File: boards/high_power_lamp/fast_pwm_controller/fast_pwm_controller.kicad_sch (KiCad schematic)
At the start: 26 parts, among them J1 Screw_Terminal_01x02, J2 Screw_Terminal_01x02, J3 Screw_Terminal_01x02, J4 Screw_Terminal_01x02, J5 Screw_Terminal_01x02, J6 Screw_Terminal_01x02, J7 Screw_Terminal_01x02, J8 Screw_Terminal_01x02, J9 Screw_Terminal_01x02, U1 4050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

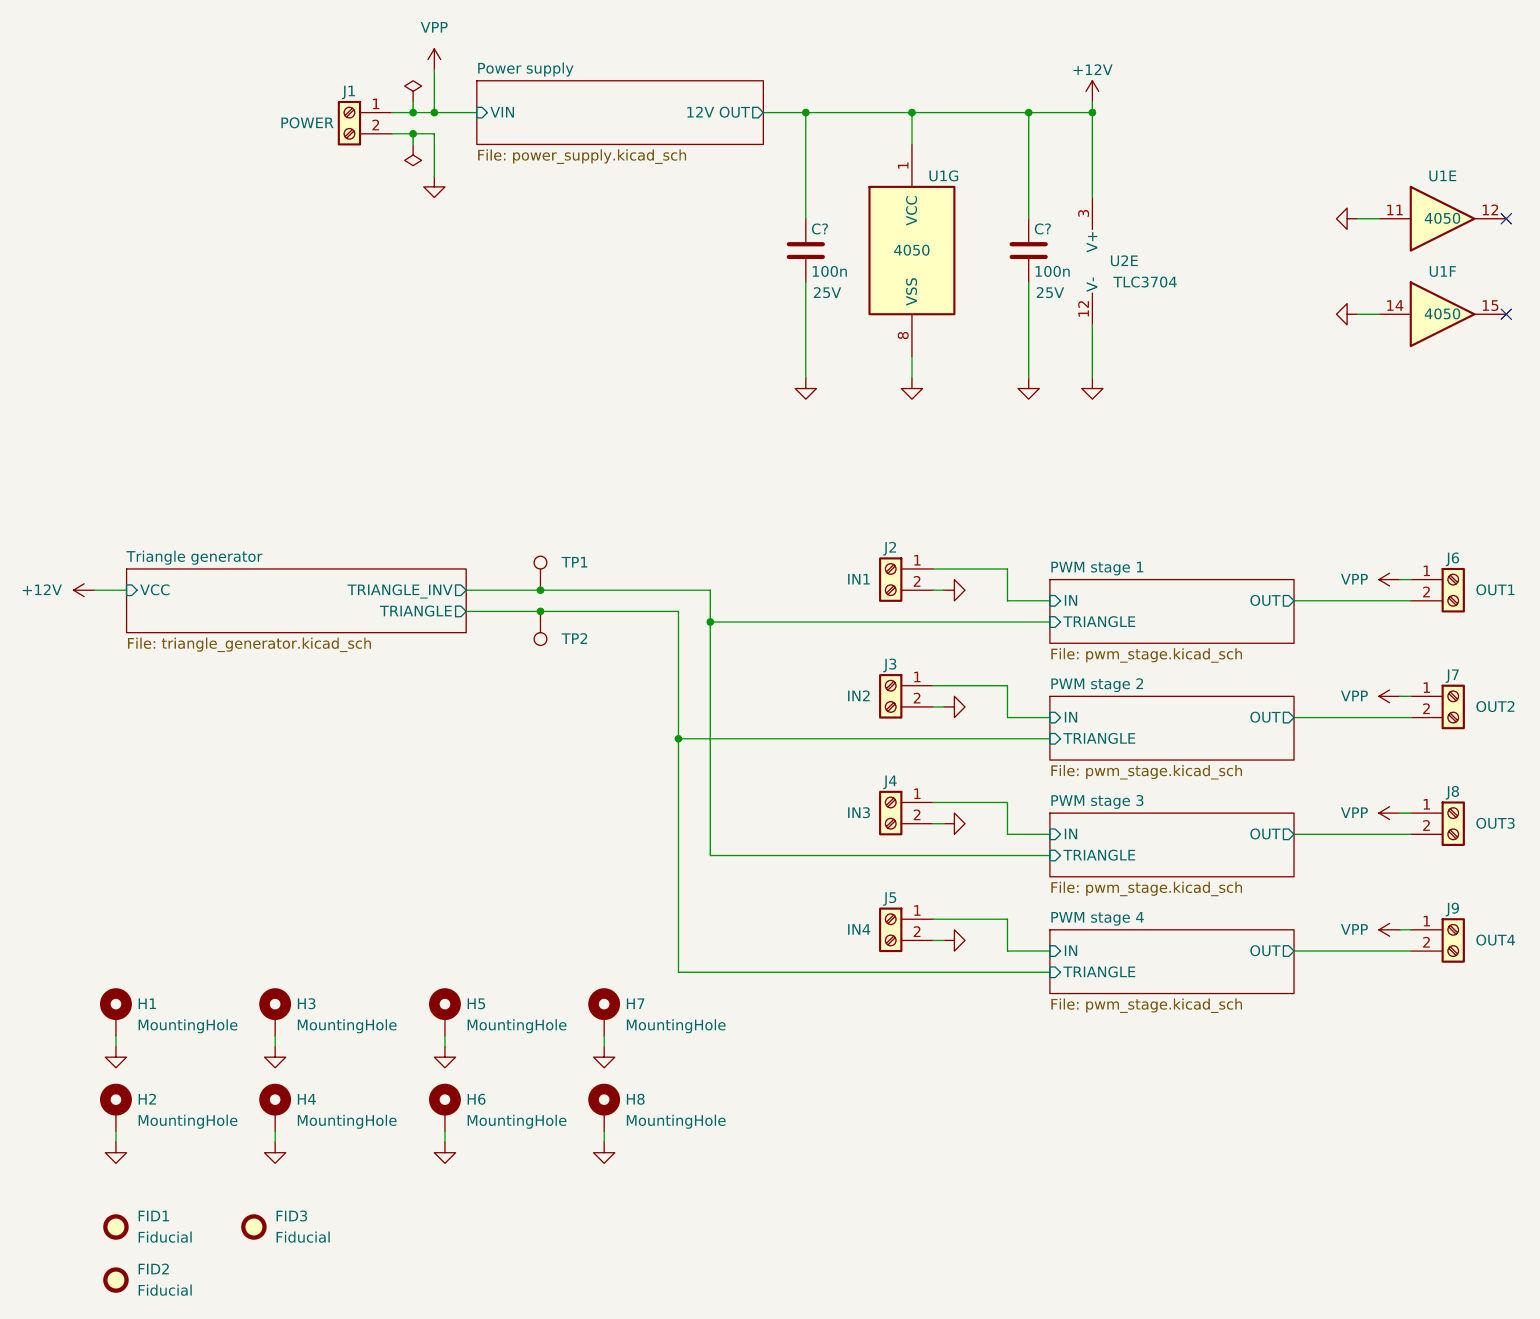
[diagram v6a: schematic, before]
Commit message: change connectors
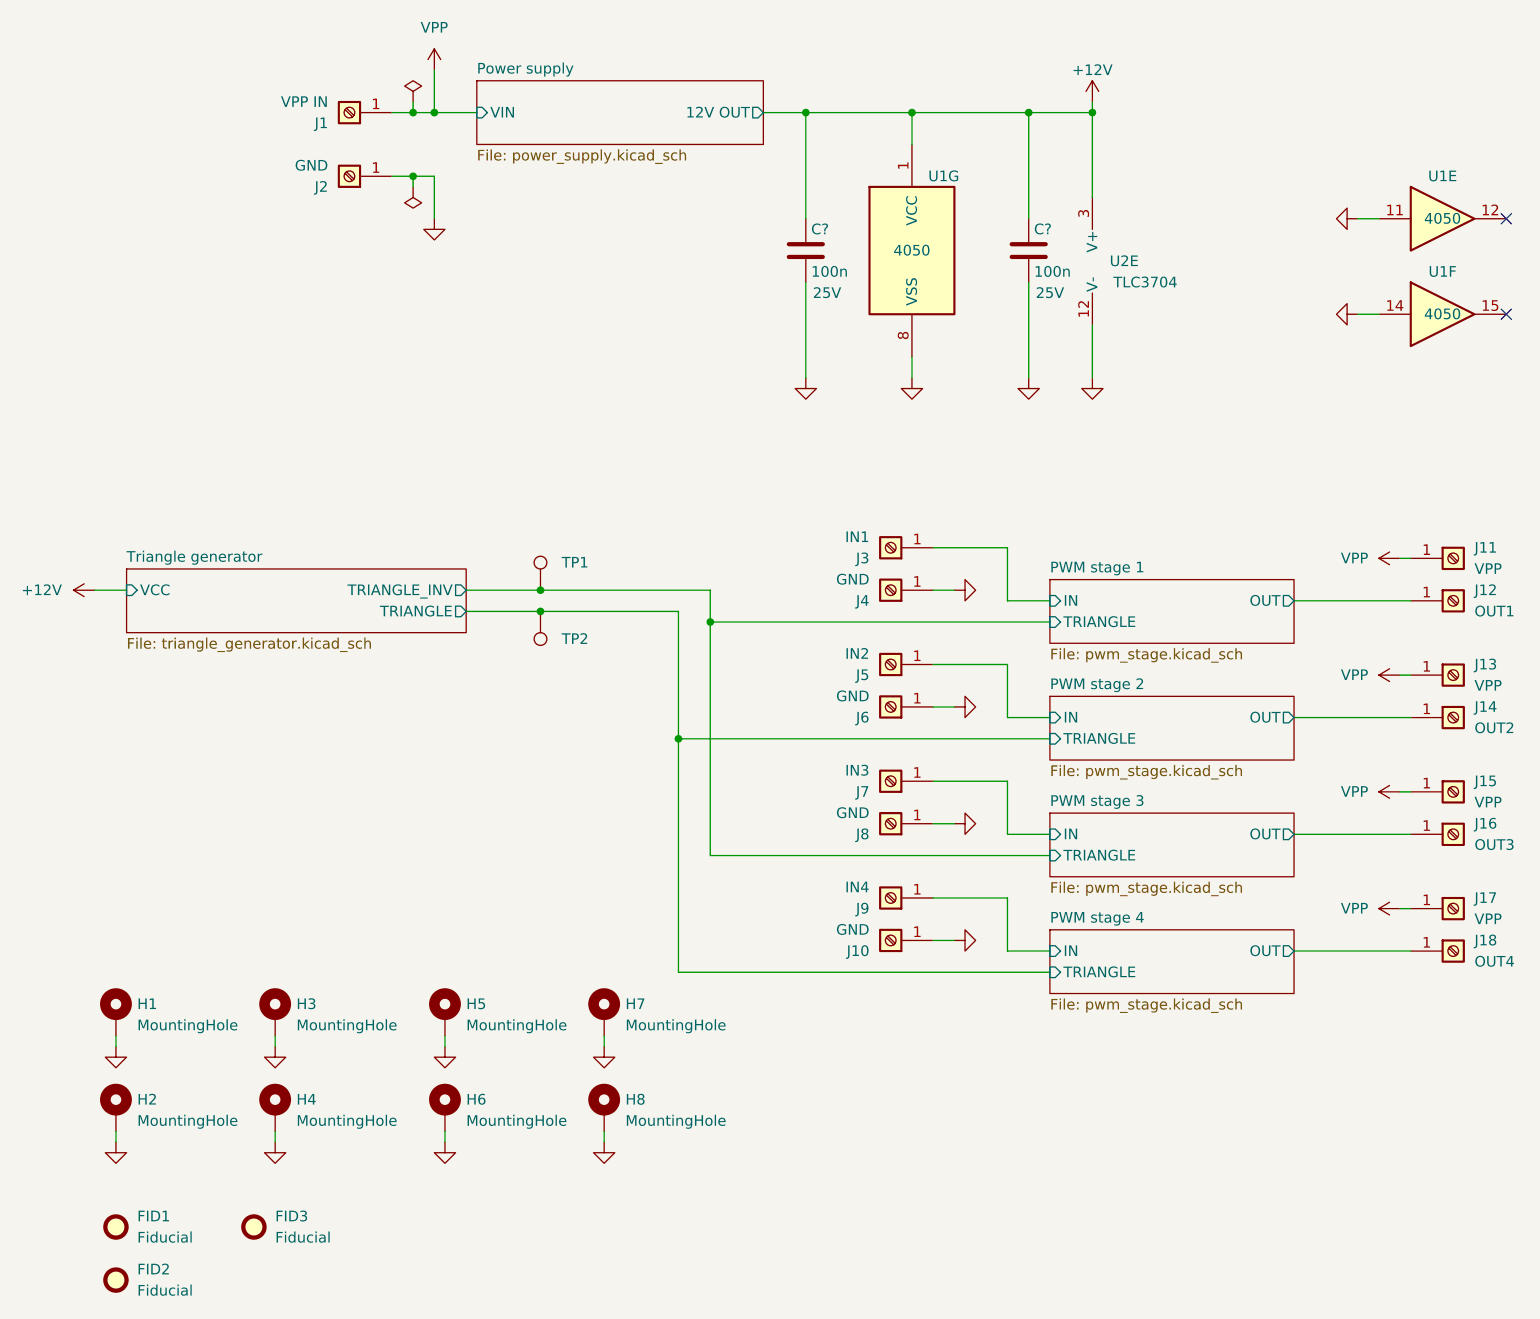
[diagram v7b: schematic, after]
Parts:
- removed J1, J2, J3, J4, J5, J6, J7, J8, J9: Screw_Terminal_01x02, TerminalBlock_Philmore:TerminalBlock_Philmore_TB132_1x02_P5.00mm_Horizontal, symbol Connector:Screw_Terminal_01x02
- added J1, J10, J11, J12, J13, J14, J15, J16, J17, J18, J2, J3, J4, J5, J6, J7, J8, J9: Screw_Terminal_01x01, connectors:1PIN_DG306, symbol Connector:Screw_Terminal_01x01
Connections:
- net GND: now also J10.1 (Pin_1), J2.1 (Pin_1), J4.1 (Pin_1), J6.1 (Pin_1), J8.1 (Pin_1)
- net PWM stage 1/IN: now also J3.1 (Pin_1)
- net PWM stage 1/OUT: now also J12.1 (Pin_1)
- net PWM stage 2/IN: now also J5.1 (Pin_1)
- net PWM stage 2/OUT: now also J14.1 (Pin_1)
- net PWM stage 3/IN: now also J7.1 (Pin_1)
- net PWM stage 3/OUT: now also J16.1 (Pin_1)
- net PWM stage 4/IN: now also J9.1 (Pin_1)
- net PWM stage 4/OUT: now also J18.1 (Pin_1)
- net VPP: now also J1.1 (Pin_1), J11.1 (Pin_1), J13.1 (Pin_1), J15.1 (Pin_1), J17.1 (Pin_1)

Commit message: finalise pcb
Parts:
- J14: Purpose OUT2 -> OUT4
- J16: Purpose OUT3 -> OUT2
- J18: Purpose OUT4 -> OUT3
- J5: Purpose IN2 -> IN4
- J7: Purpose IN3 -> IN2
- J9: Purpose IN4 -> IN3
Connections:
- net PWM stage 2/IN: now also J7.1 (Pin_1); no longer J5.1 (Pin_1)
- net PWM stage 2/OUT: now also J16.1 (Pin_1); no longer J14.1 (Pin_1)
- net PWM stage 3/IN: now also J9.1 (Pin_1); no longer J7.1 (Pin_1)
- net PWM stage 3/OUT: now also J18.1 (Pin_1); no longer J16.1 (Pin_1)
- net PWM stage 4/IN: now also J5.1 (Pin_1); no longer J9.1 (Pin_1)
- net PWM stage 4/OUT: now also J14.1 (Pin_1); no longer J18.1 (Pin_1)
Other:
- moved on the sheet: J10, J13, J14, J15, J16, J17, J18, J5, J6, J7, J8, J9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
